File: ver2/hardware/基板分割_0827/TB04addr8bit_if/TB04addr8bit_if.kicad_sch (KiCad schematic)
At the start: 11 parts, among them J1 Conn_02x20_Odd_Even, J101 USB_C_Receptacle_PowerOnly_6P, J1602 Screw_Terminal_01x02, J4 Conn_02x10_Odd_Even, SW101 SW_SPDT

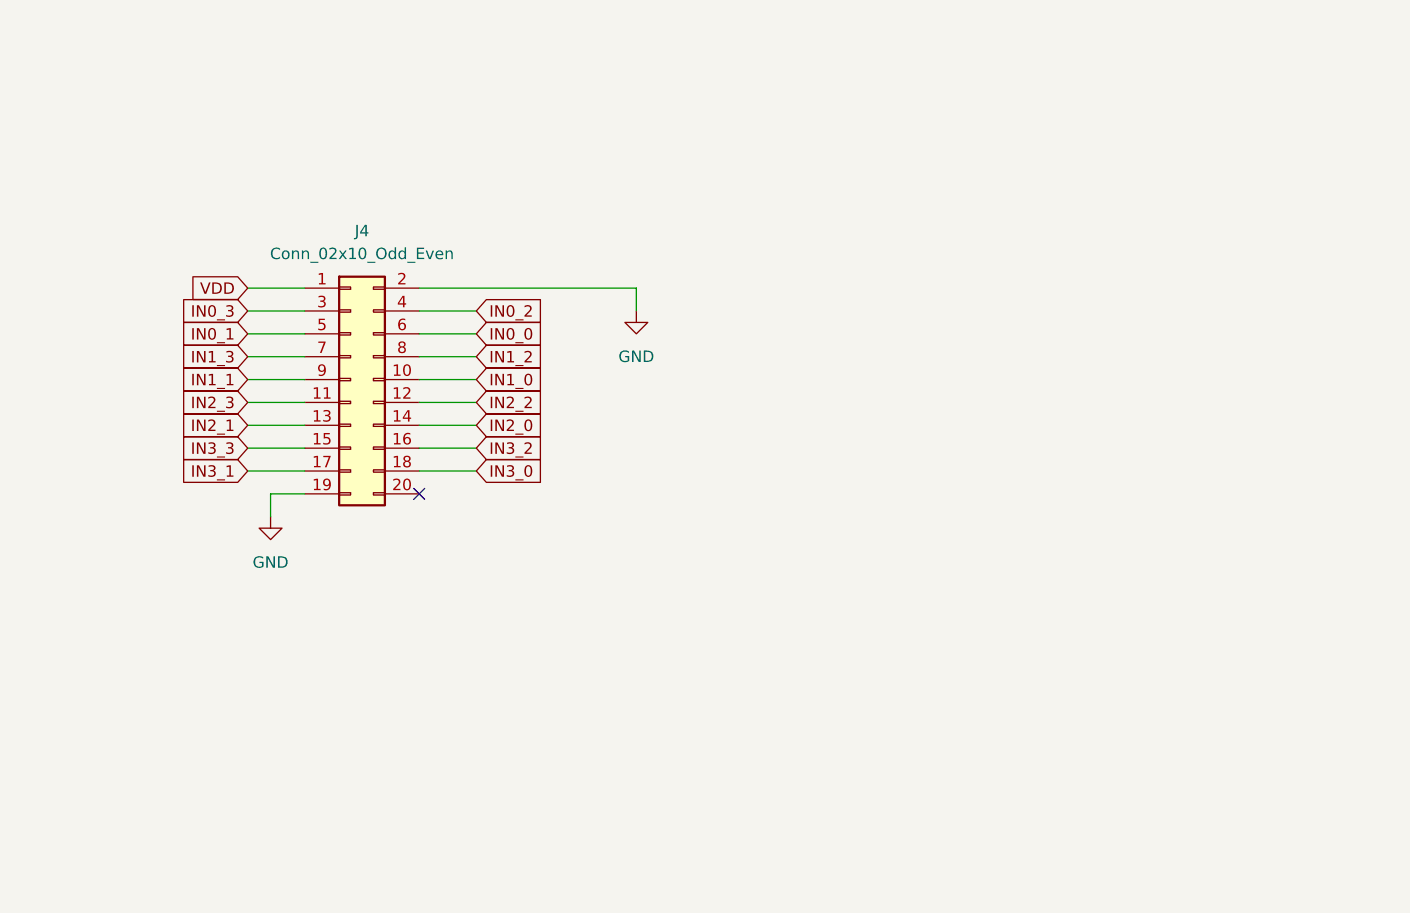
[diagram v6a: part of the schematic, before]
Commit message: ver2: デザインルールを3枚へコピー／制御板の配置を決定(200x180へ拡大)
デザインルール(キャリアで決めた値を_ctrl/_alu/_ifへ):
- 信号0.2mm・電源0.8mm・クリアランス0.2mm・ビア0.6/0.3
- 銅箔-基板端0.5mm、ゾーン最小クリアランス0.5mm

制御板の配置:
- 200x135では部品が55mm分あふれるため200x180へ拡大($16.9->$21.3)
- ブロックの左右はケーブルの向きで決定(J1=IF板/J2,J3=演算板への
  接続本数の差で並べ、ROM_ALUを演算板側の右端へ)
- 並び: ram,addrMUX -> PC_aluMux,sp,addrDecord -> gates -> Decoder -> ROM_ALU
- パスコンは全34ICの1番ピンと電源ピンの間(DIPの上辺)に配置
- 表示8桁を下端に25mmピッチ一列、ケーブルは左右端、電源入口は上端

検証: 外形はみ出し0・courtyard重なり0・パスコン34/34
DRC違反はシルク3件のみ(未配線499は配線前のため)

同梱: 並行して行われた回路図編集(キャリア用2x10を廃し2x5直挿しへ。
制御板はJ5削除、IF板はJ4->J10-J13)

Co-Authored-By: Claude Opus 5 <noreply@anthropic.com>
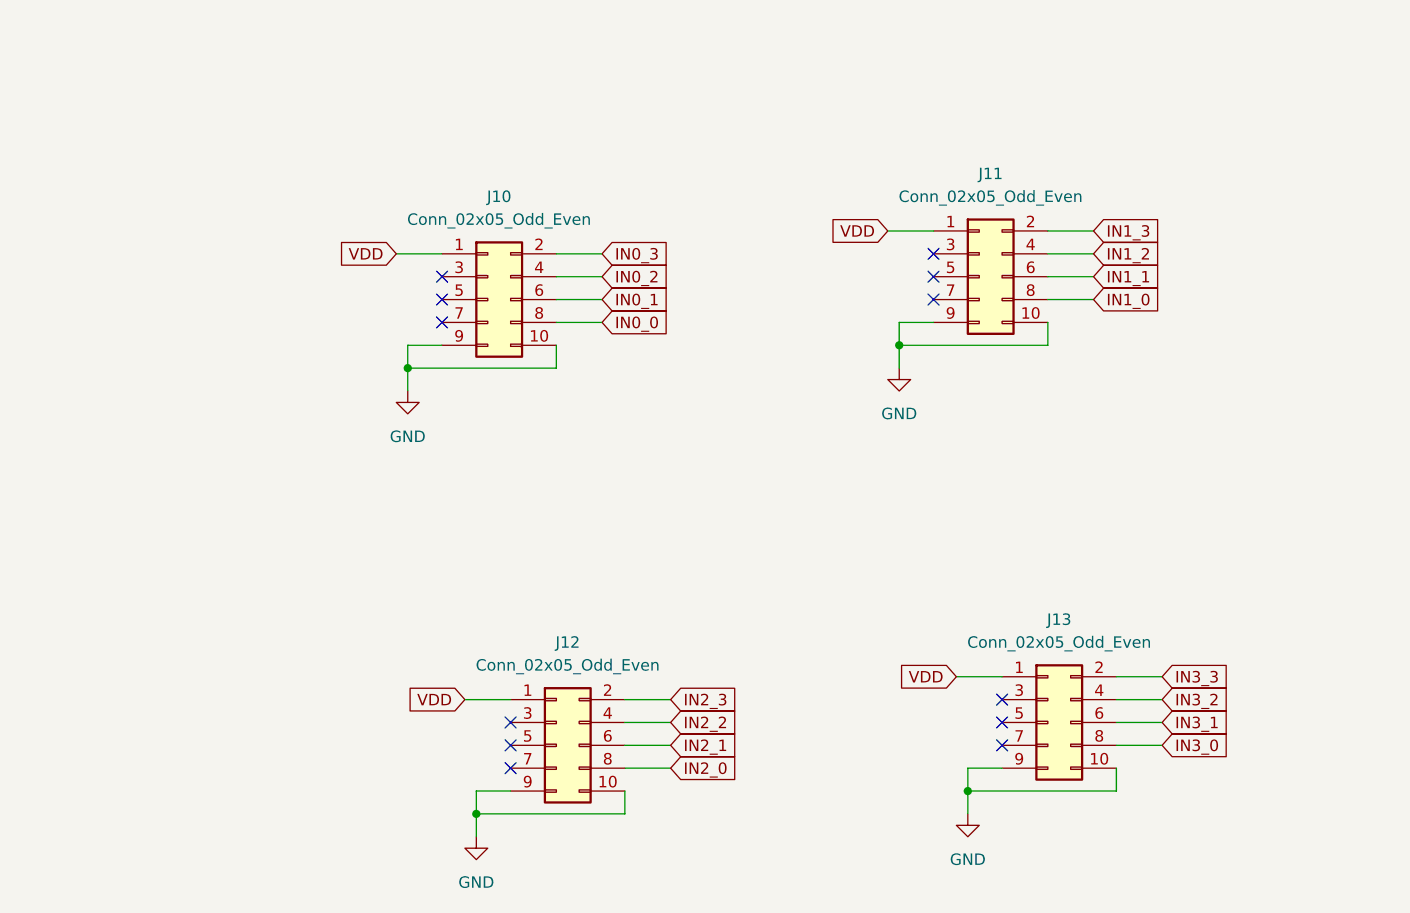
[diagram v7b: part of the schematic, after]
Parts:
- removed J4: Conn_02x10_Odd_Even, Connector_PinSocket_2.54mm:PinSocket_2x10_P2.54mm_Vertical, symbol Connector_Generic:Conn_02x10_Odd_Even
- added J10, J11, J12, J13: Conn_02x05_Odd_Even, Connector_PinSocket_2.54mm:PinSocket_2x05_P2.54mm_Vertical, symbol Connector_Generic:Conn_02x05_Odd_Even
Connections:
- net GND: now also J10.10 (Pin_10), J10.9 (Pin_9), J11.10 (Pin_10), J11.9 (Pin_9), J12.10 (Pin_10), J12.9 (Pin_9), J13.10 (Pin_10), J13.9 (Pin_9)
- net IN0_0: now also J10.8 (Pin_8)
- net IN0_1: now also J10.6 (Pin_6)
- net IN0_2: now also J10.4 (Pin_4)
- net IN0_3: now also J10.2 (Pin_2)
- net IN1_0: now also J11.8 (Pin_8)
- net IN1_1: now also J11.6 (Pin_6)
- net IN1_2: now also J11.4 (Pin_4)
- net IN1_3: now also J11.2 (Pin_2)
- net IN2_0: now also J12.8 (Pin_8)
- net IN2_1: now also J12.6 (Pin_6)
- net IN2_2: now also J12.4 (Pin_4)
- net IN2_3: now also J12.2 (Pin_2)
- net IN3_0: now also J13.8 (Pin_8)
- net IN3_1: now also J13.6 (Pin_6)
- net IN3_2: now also J13.4 (Pin_4)
- net IN3_3: now also J13.2 (Pin_2)
- net VDD: now also J10.1 (Pin_1), J11.1 (Pin_1), J12.1 (Pin_1), J13.1 (Pin_1)
- no-connect marks 8 -> 19
